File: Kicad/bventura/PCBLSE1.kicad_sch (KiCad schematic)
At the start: 83 parts, among them IC1 LM339D, IC2 IR2301SPBF, IC3 IR2301SPBF, IC4 IR2301SPBF, IC5 LMS8117AMP-3.3_NOPB, J1 Conn_02x10_Counter_Clockwise, J10 Conn_01x04, J11 Conn_01x04, J12 Conn_01x04, J13 Conn_01x05, J14 Conn_01x02, J15 Conn_01x02_Pin, J16 Conn_01x04, J17 Conn_01x02, J18 Conn_01x04, J2 Conn_02x10_Counter_Clockwise, J3 Conn_01x02, J4 Conn_01x02, J5 Conn_01x02, J6 Conn_01x02, J7 Conn_01x03, J8 Conn_01x03, J9 Conn_01x05, Q1 Q_NMOS_GDS, Q2 Q_NMOS_GDS, Q3 Q_NMOS_GDS, Q4 Q_NMOS_GDS, Q5 Q_NMOS_GDS, Q7 Q_NMOS_GDS, U1 L7805

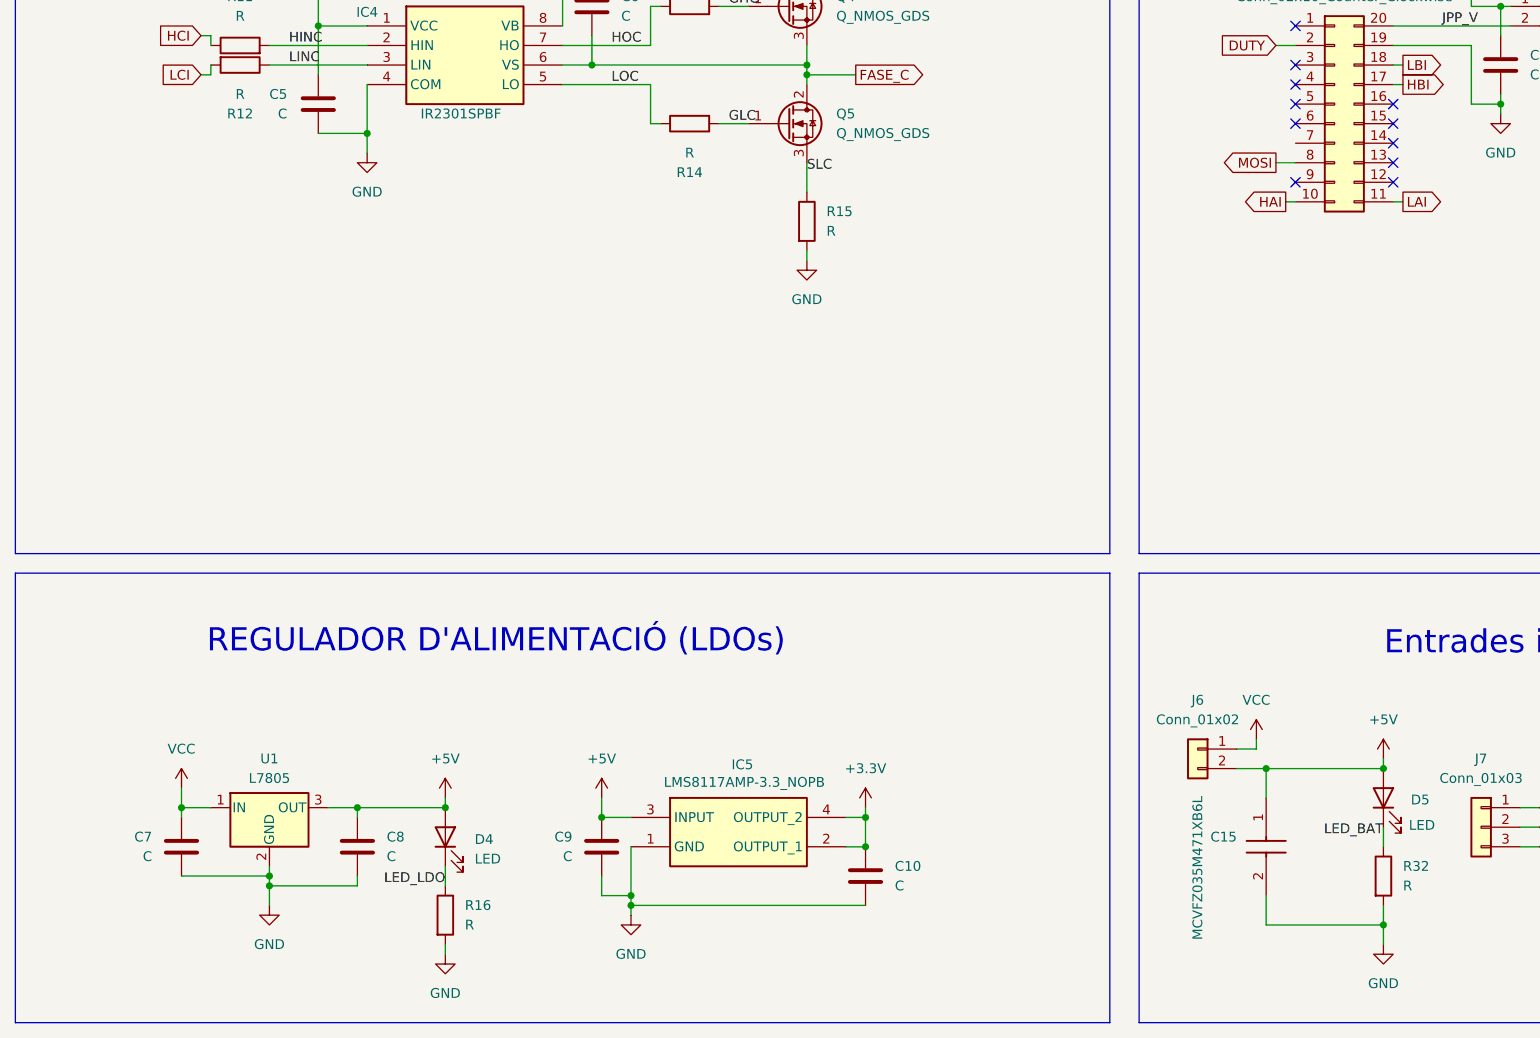
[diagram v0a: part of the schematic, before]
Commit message: Errors corregits
Errors corregits de l'esquema i nou placement dels drivers de potència. DRC esquema 3 errors, relacionats amb el power flag.
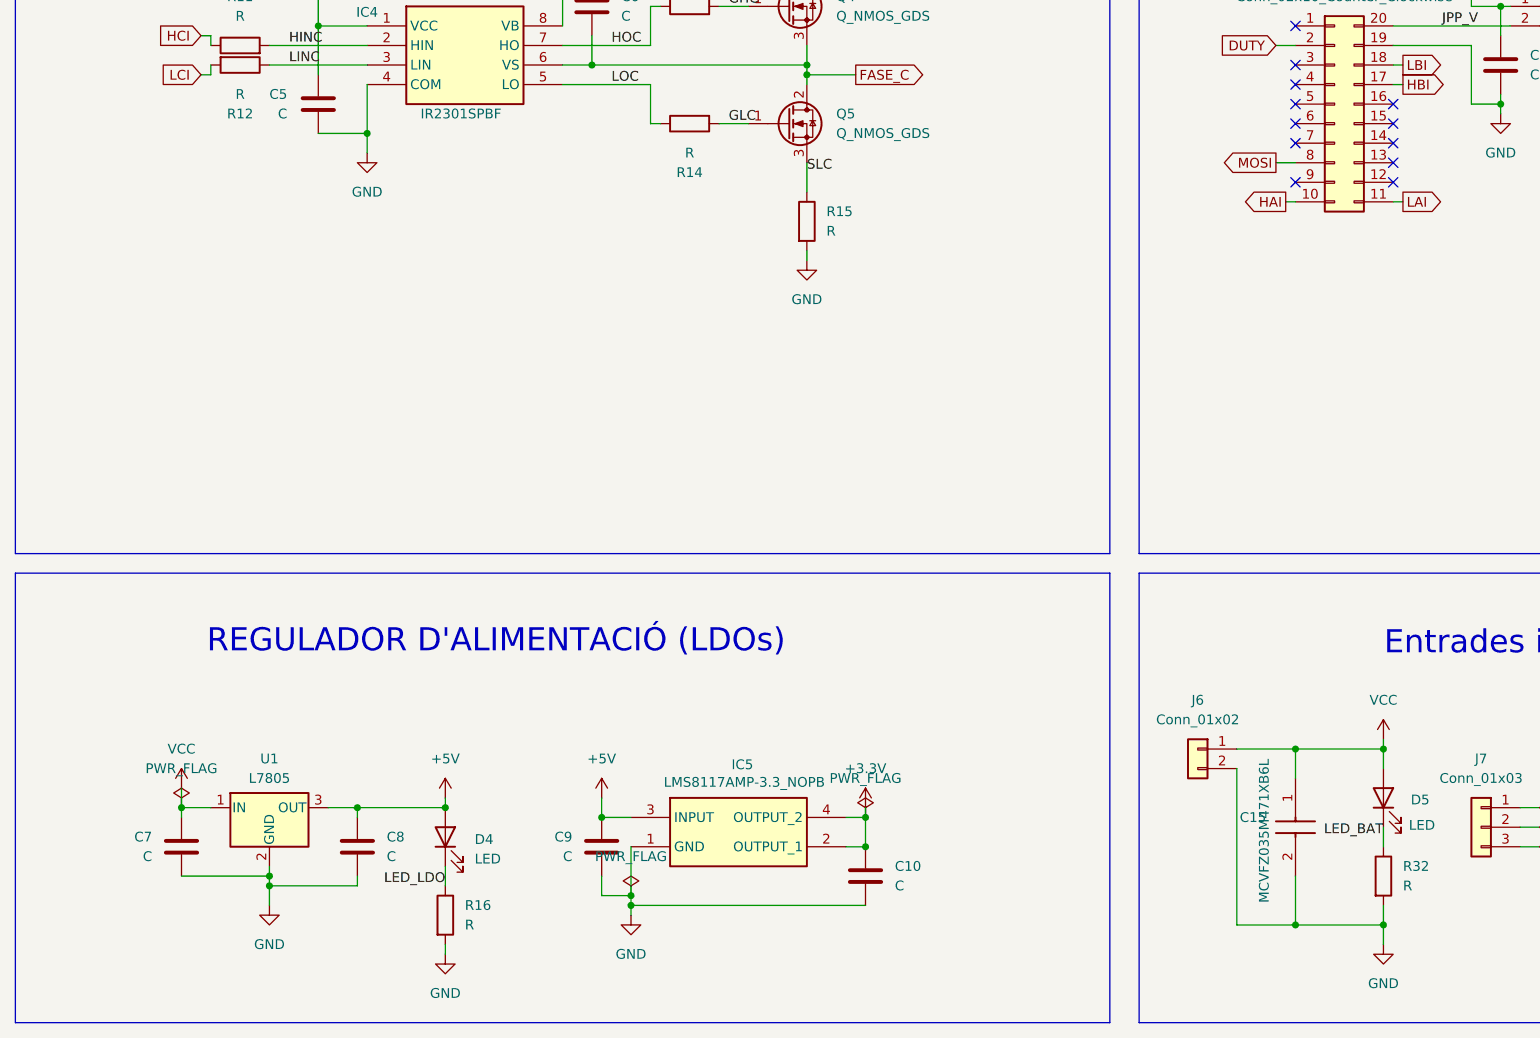
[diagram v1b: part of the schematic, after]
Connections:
- net +5V: no longer C15.1 (+), D5.2 (A), J6.2 (Pin_2)
- net GND: now also J6.2 (Pin_2)
- net VCC: now also C15.1 (+), D5.2 (A)
- no-connect marks 26 -> 27
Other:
- moved on the sheet: C15

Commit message: Add files via upload
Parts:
- removed J18: Conn_01x04, Connector_PinSocket_2.54mm:PinSocket_1x04_P2.54mm_Vertical, symbol Connector_Generic:Conn_01x04
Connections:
- net BMEFA_ZERO: now also J2.6 (Pin_6); no longer J2.1 (Pin_1)
- net BMEFB_ZERO: now also J2.12 (Pin_12); no longer J2.2 (Pin_2)
- net BMEFC_ZERO: now also J1.11 (Pin_11); no longer J2.3 (Pin_3)
- net DUTY: now also J1.4 (Pin_4); no longer J1.2 (Pin_2)
- net GND: now also J1.3 (Pin_3); no longer J1.19 (Pin_19)
- net HAI: now also J2.8 (Pin_8); no longer J1.10 (Pin_10)
- net HBI: now also J1.7 (Pin_7); no longer J1.17 (Pin_17)
- net HCI: now also J2.2 (Pin_2); no longer J2.5 (Pin_5)
- net JPP_V: now also J1.1 (Pin_1); no longer J1.20 (Pin_20)
- net LAI: now also J2.10 (Pin_10); no longer J1.11 (Pin_11)
- net LBI: now also J2.4 (Pin_4); no longer J1.18 (Pin_18)
- net LCI: now also J1.5 (Pin_5); no longer J2.4 (Pin_4)
- net MISO: now also J2.15 (Pin_15); no longer J2.13 (Pin_13)
- net MOSI: now also J1.16 (Pin_16); no longer J1.8 (Pin_8)
- net SCLK: now also J2.19 (Pin_19); no longer J2.11 (Pin_11)
- net /SS: now also J2.17 (Pin_17); no longer J2.12 (Pin_12)
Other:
- note added: "DUTY I NODE NEUTRE"
- note removed: "FASE REDUÏDA, DUTY I NODE NEUTRE"
- moved on the sheet: J1, J14, J15, J17

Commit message: Add files via upload
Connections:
- net BMEFB_ZERO: now also J1.13 (Pin_13); no longer J2.12 (Pin_12)
- net HAI: now also J2.4 (Pin_4); no longer J2.8 (Pin_8)
- net HBI: now also J2.10 (Pin_10); no longer J1.7 (Pin_7)
- net HCI: now also J1.5 (Pin_5); no longer J2.2 (Pin_2)
- net LAI: now also J2.2 (Pin_2); no longer J2.10 (Pin_10)
- net LBI: now also J2.8 (Pin_8); no longer J2.4 (Pin_4)
- net LCI: now also J1.7 (Pin_7); no longer J1.5 (Pin_5)
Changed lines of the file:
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@@
 	)
 	(no_connect
+		(at 265.43 170.18)
+	)
+	(no_connect
 		(at 265.43 157.48)
 	)
@@
 	)
 	(no_connect
+		(at 266.7 172.72)
+	)
+	(no_connect
 		(at 217.17 162.56)
 	)
@@
 	)
 	(no_connect
-		(at 217.17 172.72)
-	)
-	(no_connect
 		(at 217.17 157.48)
 	)
@@
 		(at 217.17 175.26)
 	)
-	(no_connect
-		(at 265.43 170.18)
-	)
 	(wire
 		(pts
@@
 		)
 	)
-	(global_label "MOSI"
-		(shape input)
-		(at 267.97 254 0)
+	(global_label "LCI"
+		(shape output)
+		(at 201.93 170.18 180)
 		(fields_autoplaced yes)
 		(effects
@@
 				(size 1.27 1.27)
 			)
-			(justify left)
+			(justify right)
 		)
 		(property "Intersheetrefs" "${INTERSHEET_REFS}"
-			(at 275.5514 254 0)
+			(at 196.0419 170.18 0)
 			(effects
 				(font
 					(size 1.27 1.27)
 				)
-				(justify left)
+				(justify right)
 				(hide yes)
 			)
 		)
 	)
-	(global_label "FASE_B_RED"
-		(shape input)
-		(at 273.05 83.82 180)
+	(global_label "LAI"
+		(shape output)
+		(at 250.19 154.94 180)
 		(fields_autoplaced yes)
 		(effects
@@
 		)
 		(property "Intersheetrefs" "${INTERSHEET_REFS}"
-			(at 258.6349 83.82 0)
+			(at 244.4833 154.94 0)
 			(effects
 				(font
@@
 	)
 	(global_label "MOSI"
-		(shape output)
-		(at 219.71 165.1 0)
+		(shape input)
+		(at 267.97 254 0)
 		(fields_autoplaced yes)
 		(effects
@@
 		)
 		(property "Intersheetrefs" "${INTERSHEET_REFS}"
-			(at 227.2914 165.1 0)
+			(at 275.5514 254 0)
 			(effects
 				(font
@@
 		)
 	)
-	(global_label "LCI"
-		(shape output)
-		(at 201.93 165.1 180)
+	(global_label "BMEFB_ZERO"
+		(shape input)
+		(at 217.17 172.72 0)
+		(fields_autoplaced yes)
+		(effects
+			(font
+				(size 1.27 1.27)
+			)
+			(justify left)
+		)
+		(property "Intersheetrefs" "${INTERSHEET_REFS}"
+			(at 232.3108 172.72 0)
+			(effects
+				(font
+					(size 1.27 1.27)
+				)
+				(justify left)
+				(hide yes)
+			)
+		)
+	)
+	(global_label "FASE_B_RED"
+		(shape input)
+		(at 273.05 83.82 180)
 		(fields_autoplaced yes)
 		(effects
@@
 		)
 		(property "Intersheetrefs" "${INTERSHEET_REFS}"
-			(at 196.0419 165.1 0)
+			(at 258.6349 83.82 0)
 			(effects
 				(font
@@
 		)
 	)
-	(global_label "FASE_C"
-		(shape input)
-		(at 215.9 257.81 0)
+	(global_label "MOSI"
+		(shape output)
+		(at 219.71 165.1 0)
 		(fields_autoplaced yes)
 		(effects
@@
 		)
 		(property "Intersheetrefs" "${INTERSHEET_REFS}"
-			(at 225.6585 257.81 0)
+			(at 227.2914 165.1 0)
 			(effects
 				(font
@@
 	)
 	(global_label "FASE_C"
-		(shape output)
-		(at 127 157.48 0)
+		(shape input)
+		(at 215.9 257.81 0)
 		(fields_autoplaced yes)
 		(effects
@@
 		)
 		(property "Intersheetrefs" "${INTERSHEET_REFS}"
-			(at 136.7585 157.48 0)
+			(at 225.6585 257.81 0)
 			(effects
 				(font
@@
 		)
 	)
-	(global_label "HCI"
+	(global_label "FASE_C"
 		(shape output)
-		(at 250.19 154.94 180)
+		(at 127 157.48 0)
 		(fields_autoplaced yes)
 		(effects
@@
 				(size 1.27 1.27)
 			)
-			(justify right)
+			(justify left)
 		)
 		(property "Intersheetrefs" "${INTERSHEET_REFS}"
-			(at 243.9995 154.94 0)
+			(at 136.7585 157.48 0)
 			(effects
 				(font
 					(size 1.27 1.27)
 				)
-				(justify right)
+				(justify left)
 				(hide yes)
 			)
@@
 		)
 	)
+	(global_label "HBI"
+		(shape output)
+		(at 251.46 175.26 180)
+		(fields_autoplaced yes)
+		(effects
+			(font
+				(size 1.27 1.27)
+			)
+			(justify right)
+		)
+		(property "Intersheetrefs" "${INTERSHEET_REFS}"
+			(at 245.2695 175.26 0)
+			(effects
+				(font
+					(size 1.27 1.27)
+				)
+				(justify right)
+				(hide yes)
+			)
+		)
+	)
 	(global_label "GHB"
 		(shape input)
@@
 		)
 	)
-	(global_label "BMEFB_ZERO"
-		(shape input)
-		(at 266.7 172.72 0)
+	(global_label "LBI"
+		(shape output)
+		(at 251.46 170.18 180)
 		(fields_autoplaced yes)
 		(effects
@@
 				(size 1.27 1.27)
 			)
-			(justify left)
+			(justify right)
 		)
 		(property "Intersheetrefs" "${INTERSHEET_REFS}"
-			(at 281.8408 172.72 0)
+			(at 245.5719 170.18 0)
 			(effects
 				(font
 					(size 1.27 1.27)
 				)
-				(justify left)
+				(justify right)
 				(hide yes)
 			)
@@
 		)
 	)
+	(global_label "HCI"
+		(shape output)
+		(at 201.93 165.1 180)
+		(fields_autoplaced yes)
+		(effects
+			(font
+				(size 1.27 1.27)
+			)
+			(justify right)
+		)
+		(property "Intersheetrefs" "${INTERSHEET_REFS}"
+			(at 195.7395 165.1 0)
+			(effects
+				(font
+					(size 1.27 1.27)
+				)
+				(justify right)
+				(hide yes)
+			)
+		)
+	)
 	(global_label "MISO"
 		(shape input)
@@
 		)
 	)
-	(global_label "LBI"
+	(global_label "HAI"
 		(shape output)
 		(at 251.46 160.02 180)
@@
 		)
 		(property "Intersheetrefs" "${INTERSHEET_REFS}"
-			(at 245.5719 160.02 0)
+			(at 245.4509 160.02 0)
 			(effects
 				(font
@@
 		)
 	)
-	(global_label "HBI"
-		(shape output)
-		(at 201.93 170.18 180)
-		(fields_autoplaced yes)
-		(effects
-			(font
-				(size 1.27 1.27)
-			)
-			(justify right)
-		)
-		(property "Intersheetrefs" "${INTERSHEET_REFS}"
-			(at 195.7395 170.18 0)
-			(effects
-				(font
-					(size 1.27 1.27)
-				)
-				(justify right)
-				(hide yes)
-			)
-		)
-	)
-	(global_label "HAI"
-		(shape output)
-		(at 251.46 170.18 180)
-		(fields_autoplaced yes)
-		(effects
-			(font
-				(size 1.27 1.27)
-			)
-			(justify right)
-		)
-		(property "Intersheetrefs" "${INTERSHEET_REFS}"
-			(at 245.4509 170.18 0)
-			(effects
-				(font
-					(size 1.27 1.27)
-				)
-				(justify right)
-				(hide yes)
-			)
-		)
-	)
 	(global_label "FASE_A"
 		(shape input)
@@
 				(hide yes)
 			)
-		)
-	)
-	(global_label "LAI"
-		(shape output)
-		(at 251.46 175.26 180)
-		(fields_autoplaced yes)
-		(effects
-			(font
-				(size 1.27 1.27)
-			)
-			(justify right)
-		)
-		(property "Intersheetrefs" "${INTERSHEET_REFS}"
-			(at 245.7533 175.26 0)
-			(effects
-				(font
-					(size 1.27 1.27)
-				)
-				(justify right)
-				(hide yes)
-			)

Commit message: versió final kicad
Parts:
- J1, J2: footprint Connector_PinSocket_2.54mm:PinSocket_2x10_P2.54mm_Vertical -> Connector_PinHeader_2.54mm:PinHeader_2x10_P2.54mm_Vertical
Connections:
- net BMEFA_ZERO: now also J2.5 (Pin_5); no longer J2.6 (Pin_6)
- net BMEFB_ZERO: now also J1.14 (Pin_14); no longer J1.13 (Pin_13)
- net BMEFC_ZERO: now also J1.12 (Pin_12); no longer J1.11 (Pin_11)
- net DUTY: now also J1.3 (Pin_3); no longer J1.4 (Pin_4)
- net GND: now also J1.4 (Pin_4); no longer J1.3 (Pin_3)
- net HAI: now also J2.3 (Pin_3); no longer J2.4 (Pin_4)
- net HBI: now also J2.9 (Pin_9); no longer J2.10 (Pin_10)
- net HCI: now also J1.6 (Pin_6); no longer J1.5 (Pin_5)
- net JPP_V: now also J1.2 (Pin_2); no longer J1.1 (Pin_1)
- net LAI: now also J2.1 (Pin_1); no longer J2.2 (Pin_2)
- net LBI: now also J2.7 (Pin_7); no longer J2.8 (Pin_8)
- net LCI: now also J1.8 (Pin_8); no longer J1.7 (Pin_7)
- net MISO: now also J2.16 (Pin_16); no longer J2.15 (Pin_15)
- net MOSI: now also J1.15 (Pin_15); no longer J1.16 (Pin_16)
- net SCLK: now also J2.20 (Pin_20); no longer J2.19 (Pin_19)
- net /SS: now also J2.18 (Pin_18); no longer J2.17 (Pin_17)
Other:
- note added: "Capacitats de bypass C12,C11,C13."
- note added: "Comporadors per detectar el pas per zero."
- note added: "Comunicació SPI per LSE-2: MISO - PA4 /SS - PA3 SCLK - PA2 MOSI - PA5"
- note added: "Configuració de xarxa estrella per definir el node neutre. Divisors de tensió per reduïr la tensió dels senyals de la fase."
- note added: "Connector SPI per LSE-2"
- note added: "Connector bateria"
- note added: "Connector sortides motor"
- note added: "Connexions per BEMF: BEMFA_ZERO - PB3 BEMFB_ZERO - PE1 BEMFC_ZERO - PD3"
- note added: "Connexió Potenciòmetre: DUTY - PB5"
- note added: "Connexió amb PWM: HAI - PF3 LAI - PF2 HBI - PC5 LBI - PC4 HCI - PD0 LCI - PD1"
- note added: "Drivers de potència per generar la fase A, fase B i fase C."
- note added: "Jumper per alimentar la placa amb el LDO +5V quan no estigui conectada"
- note added: "Potenciòmetre - Entrada ADC"
- note added: "Reducció de tensió de bateria a +5V i +3,3V per els diferents components"
- note added: "Resistències R29, R30, R31 de pull-up."
- moved on the sheet: C10, C15, C7, C8, C9, D4, D5, IC5, J15, J6, J8, J9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
